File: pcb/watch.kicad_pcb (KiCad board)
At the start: 2 copper layers, 25.4 x 25.4 mm, 26 parts, among them SW1 EVP-AA202K, SW2 EVP-AA202K, U1 ATtiny402-SS

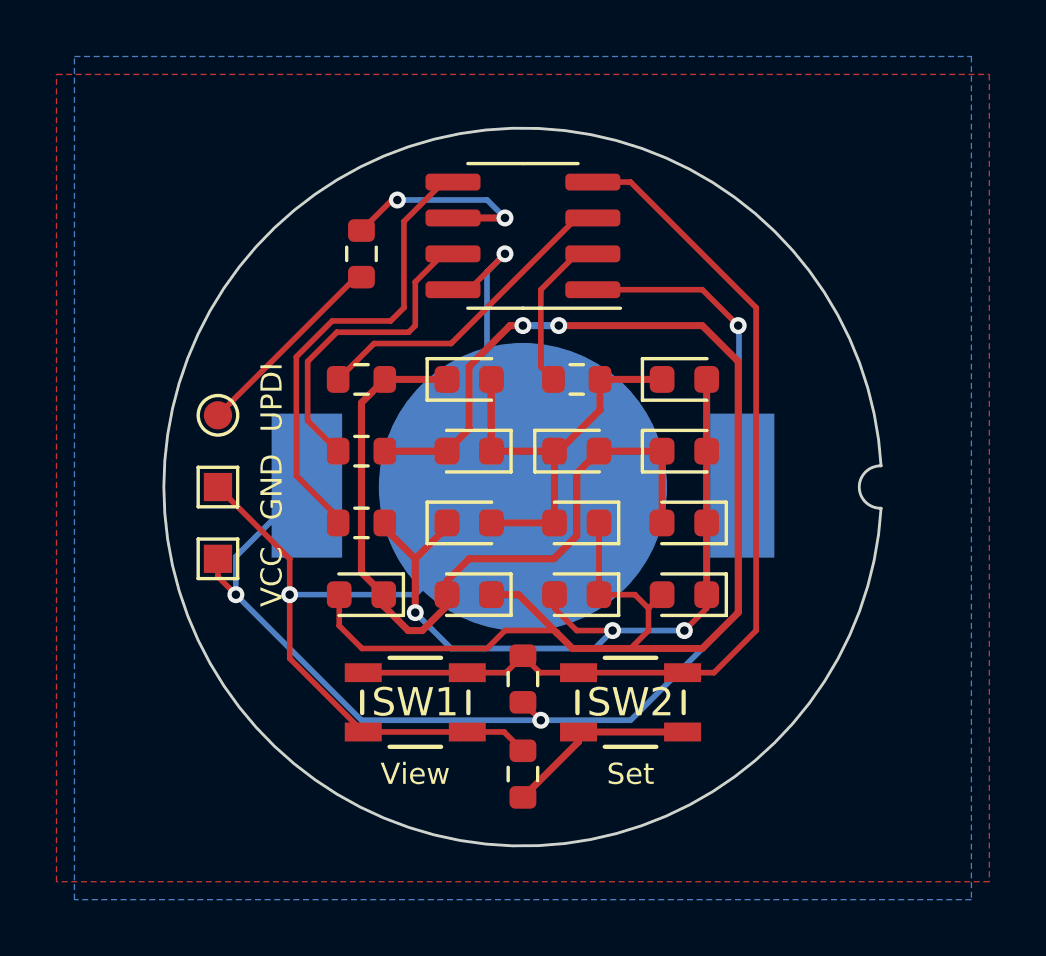
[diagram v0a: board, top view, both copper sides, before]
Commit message: Make the PCB more aesthetically pleasing
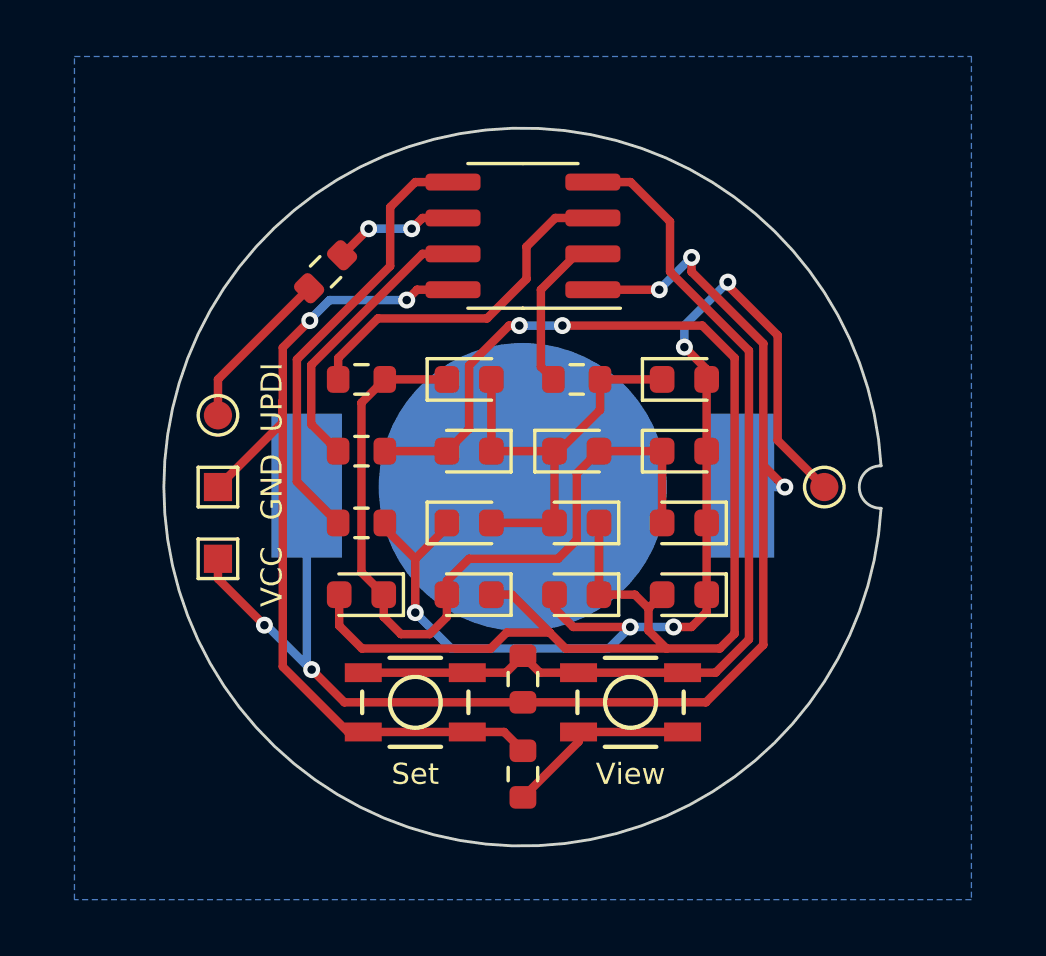
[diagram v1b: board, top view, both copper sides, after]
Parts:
- added TP4: TestPoint, TestPoint:TestPoint_Pad_D1.0mm, F.Cu at (74.2, 63.5)
- R1, R2, R3, R4: value 47 -> 47 Ω
- R5, R6: value R_Small_US -> 4.7 kΩ
- R7: value 5k7 -> 4.7 kΩ
- moved R7 1.42 mm to (56.5, 55.9), turned to -135 degrees
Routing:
- net Net-(D1-Pad2): track 27.8 -> 41.5 mm, vias 3 -> 5
- net +3.3V: track 44.4 -> 51.2 mm, vias 3 -> 5
- net GND: track 38.0 -> 31.9 mm
- net Net-(R7-Pad1): track 7.63 -> 4.47 mm
- net Net-(R7-Pad2): track 7.11 -> 5.83 mm
- net Net-(R2-Pad1): track 11.3 -> 10.1 mm
- net Net-(R4-Pad1): track 11.4 -> 12.5 mm
- net Net-(D10-Pad2): track 28.1 -> 28.7 mm
- net Net-(R1-Pad1): track 16.4 -> 15.7 mm
- removed copper zone on F.Cu, net GND
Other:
- board text added: "github.com/tux2603/watch"
